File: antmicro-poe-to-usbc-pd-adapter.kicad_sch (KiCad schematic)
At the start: 24 parts, among them J1 Bus_RJ45_5-2337992-8, J2 Bus_RJ45_5-2337992-8, J3 USB-C_WE_632723300011, Q1 PJE138K, U1 TPS2372-3RGWR, U2 LV14540DDAR, U3 STUSB4710AQ1TR, U4 IEA48003A280V-001-R

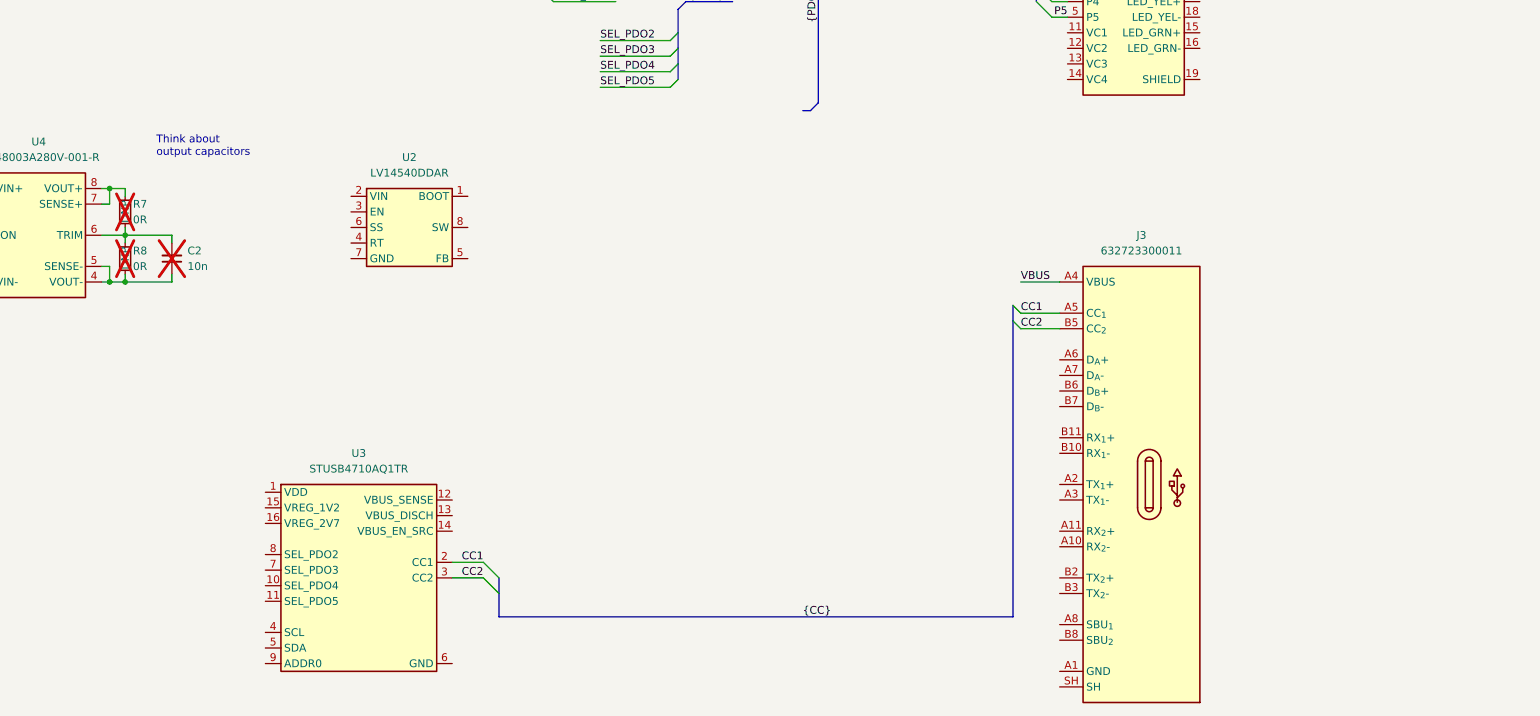
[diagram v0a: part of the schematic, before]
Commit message: [#62182] Connect LV14540
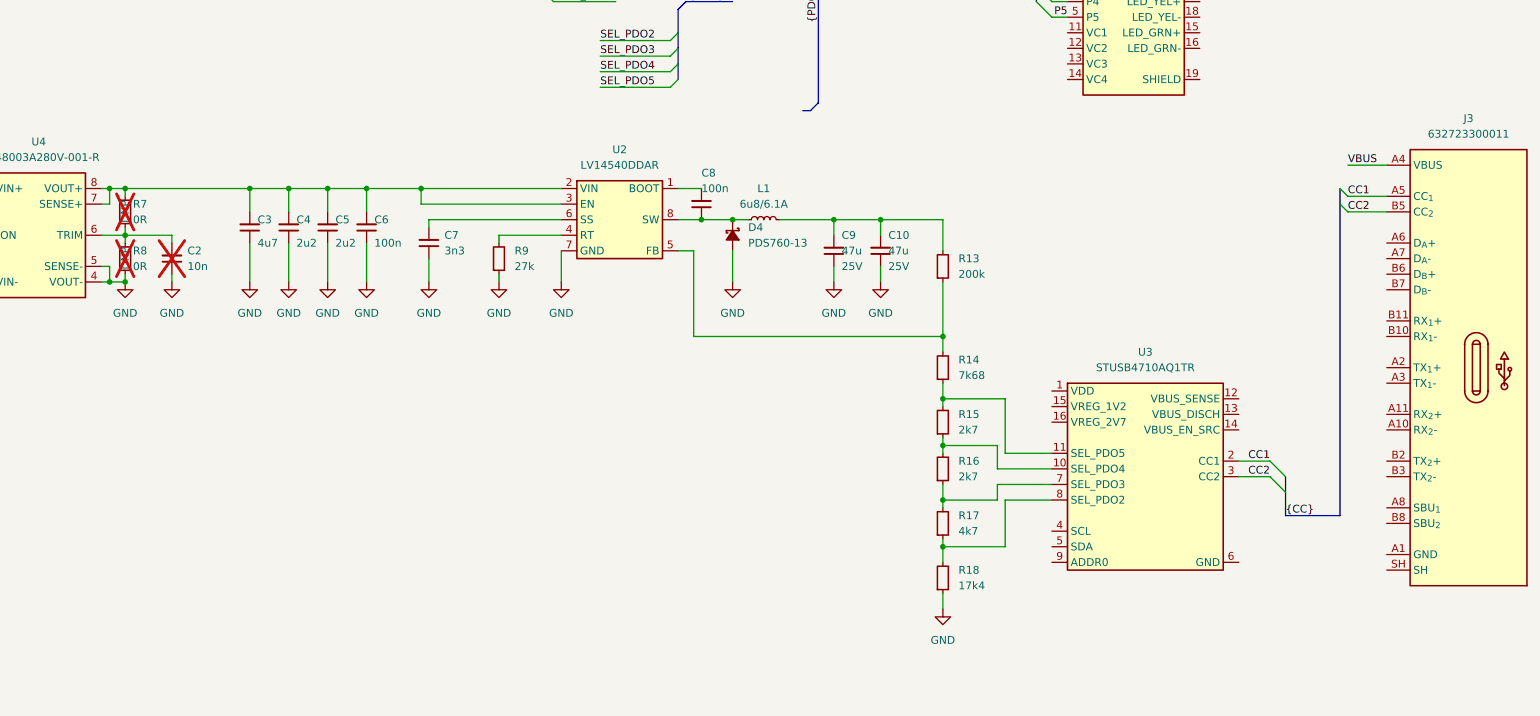
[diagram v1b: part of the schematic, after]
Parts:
- added C10, C9: C_47u_25V_1206, antmicro-footprints:C_1206_3216Metric, symbol antmicroCapacitorsmisc:C_47u_25V_1206
- added C3: C_4u7_1210_100V, antmicro-footprints:C_1210_3225Metric, symbol antmicroCapacitorsmisc:C_4u7_1210_100V
- added C4, C5: C_2u2_1210, antmicro-footprints:C_1210_3225Metric, symbol antmicroCapacitorsmisc:C_2u2_1210
- added C6, C8: C_100n_100V_X7R_0603, antmicro-footprints:C_0603_1608Metric, symbol antmicroCapacitors0603:C_100n_100V_X7R_0603
- added C7: C_3n3_0402, antmicro-footprints:C_0402_1005Metric, symbol antmicroCapacitors0402:C_3n3_0402
- added D4: PDS760, antmicro-footprints:PowerDI5, symbol antmicroDiodesRectifiersSingle:PDS760
- added L1: L_6u8_6.1A_MPS-MPL-AL5050, antmicro-footprints:L_MPS-MPL-AL5050, symbol antmicroFixedInductors:L_6u8_6.1A_MPS-MPL-AL5050
- added R13: R_200k_0402, antmicro-footprints:R_0402_1005Metric, symbol antmicroResistors0402:R_200k_0402
- added R14: R_7k68_0402, antmicro-footprints:R_0402_1005Metric, symbol antmicroResistors0402:R_7k68_0402
- added R15, R16: R_2k7_0402, antmicro-footprints:R_0402_1005Metric, symbol antmicroResistors0402:R_2k7_0402
- added R17: R_4k7_0402, antmicro-footprints:R_0402_1005Metric, symbol antmicroResistors0402:R_4k7_0402
- added R18: R_17k4_0402, antmicro-footprints:R_0402_1005Metric, symbol antmicroResistors0402:R_17k4_0402
- added R9: R_27k_0402, antmicro-footprints:R_0402_1005Metric, symbol antmicroResistors0402:R_27k_0402
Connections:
- net GND: now reaches C2.1, R8.1, U4.4 (VOUT-), U4.5 (SENSE-)
- net GND: now also U2.7 (GND), U2.9 (GND), C10.1, C3.1, C4.1, C5.1, C6.1, C7.1, C9.1, D4.2 (A), R18.1, R9.1
- net at R7.1, U4.7 (SENSE+), U4.8 (VOUT+): now also U2.2 (VIN), U2.3 (EN), C3.2, C4.2, C5.2, C6.2
- net at U3.10 (SEL_PDO4): now also R15.1, R16.2
- net at U3.11 (SEL_PDO5): now also R14.1, R15.2
- net at U3.7 (SEL_PDO3): now also R16.1, R17.2
- net at U3.8 (SEL_PDO2): now also R17.1, R18.2
- net at U2.1 (BOOT): now also C8.2
- net at U2.4 (RT): now also R9.2
- net at U2.5 (FB): now also R13.1, R14.2
- net at U2.6 (SS): now also C7.2
- net at U2.8 (SW): now also C8.1, D4.1 (C), L1.1
- new net: C10.2, C9.2, L1.2, R13.2
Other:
- note removed: "Think about output capacitors"
- moved on the sheet: J3, U2, U3

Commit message: [#62182] Add INA230, remove STUSB4710
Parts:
- removed U3: STUSB4710AQ1TR, antmicro-footprints:QFN-16_3x3mm_P0.5mm, symbol antmicroPMICPowerDistributionSwitchesLoadDrivers:STUSB4710AQ1TR
- added U3: INA230AIRGTR, antmicro-footprints:VQFN-16-1EP_3x3mm_P0.5mm_EP1.68x1.68mm, symbol antmicroPowerMeasurement:INA230AIRGTR
- added U5: FT4232H_VQFN, antmicro-footprints:QFN-56-1EP_8x8mm_P0.5mm, symbol antmicroInterfaceControllers:FT4232H_VQFN
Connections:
- new net: U3.14 (NC), U3.15 (NC), U3.16 (NC), U3.6 (NC), U3.7 (NC), U3.8 (NC)
- new net: U5.16 (V_{CCIO}), U5.36 (V_{CCIO}), U5.50 (V_{CCIO})
- new net: U5.2 (V_{CORE}), U5.31 (V_{CORE})
- new net: U5.21 (GND), U5.41 (GND), U5.45 (GND), U5.57 (GND)
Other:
- note added: "Change for tps25751"
- note added: "Figure 9 example of configuring feedback for buck converter https://www.ti.com/lit/ug/slvubj5/slvubj5.pdf?ts=1720707392282&ref_url=https%253A%252F%252Fwww.ti.com%252Ftool%252FUSB-C-PD-DUO-EVM"
- moved on the sheet: C1, C10, C2, C3, C4, C5, C6, C7, C8, C9, D1, D2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

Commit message: [#62182] Major changes in schematic
Add TPS65987D
Add FT4232H
Add 3v3 buck
Connect components
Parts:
- removed J3: USB-C_WE_632723300011, antmicro-footprints:USB-C_Receptacle_WE_632723300011, symbol antmicroUSBConnectors:USB-C_WE_632723300011
- added C11, C12: C_4u7_0402, d1600e-psu-breakout-board-footprints:0402-cap, symbol d1600e-psu-breakout-board:C_4u7_0402
- added C13, C14: C_100n_0402, d1600e-psu-breakout-board-footprints:0402-cap, symbol d1600e-psu-breakout-board:C_100n_0402
- added C15, C16: C_18p_0402, antmicro-footprints:0402-cap, symbol antmicroCapacitors0402:C_18p_0402
- added C17: C_4u7_1210_100V, antmicro-footprints:C_1210_3225Metric, symbol antmicroCapacitorsmisc:C_4u7_1210_100V
- added C18, C19: C_2u2_1210, antmicro-footprints:C_1210_3225Metric, symbol antmicroCapacitorsmisc:C_2u2_1210
- added C20, C22: C_100n_100V_X7R_0603, antmicro-footprints:C_0603_1608Metric, symbol antmicroCapacitors0603:C_100n_100V_X7R_0603
- added C21: C_3n3_0402, antmicro-footprints:C_0402_1005Metric, symbol antmicroCapacitors0402:C_3n3_0402
- added C23, C24: C_47u_25V_1206, antmicro-footprints:C_1206_3216Metric, symbol antmicroCapacitorsmisc:C_47u_25V_1206
- added C25, C27, C28: C_10u_0402, antmicro-footprints:C_0402_1005Metric, symbol antmicroCapacitors0402:C_10u_0402
- added C26: C_100n_0402, antmicro-footprints:C_0402_1005Metric, symbol antmicroCapacitors0402:C_100n_0402
- added D5: PDS760, antmicro-footprints:PowerDI5, symbol antmicroDiodesRectifiersSingle:PDS760
- added FB1, FB2, FB3: BLM18AG601SN1D, d1600e-psu-breakout-board-footprints:0603, symbol d1600e-psu-breakout-board:BLM18AG601SN1D
- added J3: USB-C_GCT_USB4105-GF-A, antmicro-footprints:USB-C_Receptacle_GCT_USB4105-GF-A, symbol antmicroUSBConnectors:USB-C_GCT_USB4105-GF-A
- added L2: L_6u8_6.1A_MPS-MPL-AL5050, antmicro-footprints:L_MPS-MPL-AL5050, symbol antmicroFixedInductors:L_6u8_6.1A_MPS-MPL-AL5050
- added R19, R20: R_4k7_0402, antmicro-footprints:R_0402_1005Metric, symbol antmicroResistors0402:R_4k7_0402
- added R21: R_12k_0402, antmicro-footprints:R_0402_1005Metric, symbol antmicroResistors0402:R_12k_0402
- added R22, R28: R_0R_0402, antmicro-footprints:R_0402_1005Metric, symbol antmicroResistors0402:R_0R_0402
- added R23: R_1k_0402, antmicro-footprints:R_0402_1005Metric, symbol antmicroResistors0402:R_1k_0402
- added R24: R_27k_0402, antmicro-footprints:R_0402_1005Metric, symbol antmicroResistors0402:R_27k_0402
- added R25: R_200k_0402, antmicro-footprints:R_0402_1005Metric, symbol antmicroResistors0402:R_200k_0402
- added R26: R_59k_0402, antmicro-footprints:R_0402_1005Metric, symbol antmicroResistors0402:R_59k_0402
- added R27: R_0R_2010, antmicro-footprints:R_2010_5025Metric, symbol antmicroResistorsmisc:R_0R_2010
- added R29, R31: R_10k_0402, antmicro-footprints:R_0402_1005Metric, symbol antmicroResistors0402:R_10k_0402
- added R30, R32: R_100k_0402, antmicro-footprints:R_0402_1005Metric, symbol antmicroResistors0402:R_100k_0402
- added U6: TPS65987DDHRSHR, antmicro-footprints:IC_TPS65987DDHRSHR, symbol antmicroInterfaceControllers:TPS65987DDHRSHR
- added U7: LV14540DDAR, antmicro-footprints:SOIC-8-1EP_3.9x4.9x1.75mm_P1.27mm_EP_vias, symbol antmicroDCDCConverters:LV14540DDAR
- added WP1: TP_SMD1MM, d1600e-psu-breakout-board-footprints:Testpoint_smd_1mm, symbol d1600e-psu-breakout-board:TP_SMD1MM
- added Y1: KX-7_12,MHz, d1600e-psu-breakout-board-footprints:KX-7, symbol d1600e-psu-breakout-board:KX-7_12,MHz
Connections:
- net GND: now also U5.10 (TEST), U5.21 (GND), U5.41 (GND), U5.45 (GND), U5.57 (GND), C15.2, C16.2, C17.1, C18.1, C19.1, C20.1, C21.1, C23.1, C24.1, C25.1, C26.2, C27.1, C28.1, D5.2 (A), FB3.2, J3.A1 (GND), J3.A12 (GND), J3.B1 (GND), J3.B12 (GND), R21.1, R24.1, R26.1, R28.1, R30.1, R32.1, U6.20 (GND), U6.45 (GND), U6.46 (GND), U6.47 (GND), U6.51 (GND), U6.59 (GND_EP), U7.7 (GND), U7.9 (GND), Y1.4
- net GNDD: now also C11.2, C12.2, C13.2, C14.2, Y1.2
- net VBUS: now also C10.2, C9.2, L1.2, R13.2
- net +28V: now reaches C3.2, C4.2, C5.2, C6.2, R7.1, U2.2 (VIN), U2.3 (EN), U4.7 (SENSE+), U4.8 (VOUT+)
- net +28V: now also C17.2, C18.2, C19.2, C20.2, U7.2 (VIN), U7.3 (EN)
- net SDA_FTDI: now reaches U3.4 (SDA)
- net SDA_FTDI: now also U5.14 (ADBUS2), R22.2
- net SCL_FTDI: now reaches U3.5 (SCL)
- net SCL_FTDI: now also U5.12 (ADBUS0), R19.1, R20.1
- net FB3: now reaches R16.1, R17.2
- net FB3: now also U6.18 (GPIO2)
- net FB2: now reaches R15.1, R16.2
- net FB2: now also U6.17 (GPIO1)
- net FB1: now reaches R14.1, R15.2
- net FB1: now also U6.16 (GPIO0)
- net FB4: now reaches R17.1, R18.2
- net FB4: now also U6.30 (GPIO3)
- net at U5.11 (~{RESET}): now also R23.2
- net at U5.13 (ADBUS1): now also R22.1
- net WP: now reaches U5.15 (ADBUS3)
- net WP: now also WP1.1
- net +3V3: now reaches U5.16 (V_{CCIO}), U5.36 (V_{CCIO}), U5.50 (V_{CCIO})
- net +3V3: now also U5.44 (V_{REGIN}), C23.2, C24.2, C25.2, C26.1, FB1.2, FB2.2, L2.2, R19.2, R20.2, R23.1, R25.2, U6.5 (VIN_3V3)
- net Vcore: now reaches U5.2 (V_{CORE}), U5.31 (V_{CORE})
- net Vcore: now also U5.43 (V_{REGOUT})
- net OSCI: now reaches U5.3 (OSCI)
- net OSCI: now also C16.1, Y1.3
- net OSCO: now reaches U5.4 (OSCO)
- net OSCO: now also C15.1, Y1.1
- net at U5.5 (V_{PHY}): now also C12.1, C14.1, FB2.1
- net at U5.6 (REF): now also R21.2
- net USB_D+: now reaches U5.7 (D-)
- net USB_D+: now also J3.A6 (D_{A}+)
- net USB_D-: now reaches U5.8 (D+)
- net USB_D-: now also J3.A7 (D_{A}-), J3.B6 (D_{B}+), J3.B7 (D_{B}-)
- net at U5.9 (V_{PLL}): now also C11.1, C13.1, FB1.1
- new net: FB3.1, J3.SH
- new net: C22.1, D5.1 (C), L2.1, U7.8 (SW)
- new net: C22.2, U7.1 (BOOT)
- new net: R25.1, R26.2, U7.5 (FB)
- new net: J3.A4 (VBUS), J3.A9 (VBUS), J3.B4 (VBUS), J3.B9 (VBUS), R27.2, U6.13 (VBUS1)
- new net: J3.A5 (CC_{1}), U6.24 (C1_CC1)
- new net: J3.B5 (CC_{2}), U6.26 (C1_CC2)
- new net: C21.2, U7.6 (SS)
- new net: R24.2, U7.4 (RT)
- new net: R27.1, U6.3 (VBUS2)
- new net DRAIN1: U6.15 (DRAIN1), U6.19 (DRAIN1), U6.58 (DRAIN1), U6.8 (DRAIN1)
- new net DRAIN2: U6.52 (DRAIN2), U6.56 (DRAIN2), U6.57 (DRAIN2), U6.7 (DRAIN2)
- new net PDC_ADCIN1: R29.2, R30.2, U6.6 (ADCIN1)
- new net PDC_ADCIN2: R31.2, R32.2, U6.10 (ADCIN2)
- new net PDC_LDO_1V8: C27.2, U6.35 (LDO_1V8)
- new net PDC_LDO_3V3: C28.2, R29.1, R31.1, U6.9 (LDO_3V3)
- new net PDC_RESET: R28.2, U6.44 (HRESET)
- no-connect marks 5 -> 40
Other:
- note added: "just connect with other pins and make pad as big as possible"
- note removed: "Change for tps25751"
- note removed: "Figure 9 example of configuring feedback for buck converter https://www.ti.com/lit/ug/slvubj5/slvubj5.pdf?ts=1720707392282&ref_url=https%253A%252F%252Fwww.ti.com%252Ftool%252FUSB-C-PD-DUO-EVM"
- moved on the sheet: C1, C10, C2, C3, C4, C5, C6, C7, C8, C9, D1, D2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

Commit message: [#62182] Connect INA230
This is first commit after Meeting #62027
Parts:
- added R33, R34, R35, R36, R37, R38, R39, R40: R_0R_0402, antmicro-footprints:R_0402_1005Metric, symbol antmicroResistors0402:R_0R_0402
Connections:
- net +3V3: now also U3.9 (Vs), R33.2, R37.2
- net GND: now also U3.10 (GND), U3.17 (EP), R36.1, R39.1
- net SCL_FTDI: now also R35.2, R40.2
- net SDA_FTDI: now also R34.2, R38.2
- net VBUS: now also U3.11 (VBUS), U3.13 (IN+)
- net A1: now reaches U3.1 (A1)
- net A1: now also R33.1, R34.1, R35.1, R36.2
- net A0: now reaches U3.2 (A0)
- net A0: now also R37.1, R38.1, R39.2, R40.1
- no-connect marks 40 -> 41
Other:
- note removed: "Read more about Ferrite Beads"
- moved on the sheet: FB3, J3, R27, U3, U6B

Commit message: [#62182] Change passives, correct gnd
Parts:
- removed C11, C12: C_4u7_0402, d1600e-psu-breakout-board-footprints:0402-cap, symbol d1600e-psu-breakout-board:C_4u7_0402
- removed C13, C14: C_100n_0402, d1600e-psu-breakout-board-footprints:0402-cap, symbol d1600e-psu-breakout-board:C_100n_0402
- removed C15, C16: C_18p_0402, antmicro-footprints:0402-cap, symbol antmicroCapacitors0402:C_18p_0402
- removed FB1, FB2, FB3: BLM18AG601SN1D, d1600e-psu-breakout-board-footprints:0603, symbol d1600e-psu-breakout-board:BLM18AG601SN1D
- removed WP1: TP_SMD1MM, d1600e-psu-breakout-board-footprints:Testpoint_smd_1mm, symbol d1600e-psu-breakout-board:TP_SMD1MM
- removed Y1: KX-7_12,MHz, d1600e-psu-breakout-board-footprints:KX-7, symbol d1600e-psu-breakout-board:KX-7_12,MHz
- added C11, C29: C_4u7_25V_0402, antmicro-footprints:C_0402_1005Metric, symbol antmicroCapacitors0402:C_4u7_25V_0402
- added C12, C30: C_100n_16V_X7R_0402, antmicro-footprints:C_0402_1005Metric, symbol antmicroCapacitors0402:C_100n_16V_X7R_0402
- added C13, C14: C_18p_0402, antmicro-footprints:C_0402_1005Metric, symbol antmicroCapacitors0402:C_18p_0402
- added FB1, FB4, FB5: FB_600Z_0.5A_Murata-BLM18AG_0603, antmicro-footprints:FB_0603_1608Metric, symbol antmicroFerriteBeadsandChips:FB_600Z_0.5A_Murata-BLM18AG_0603
- added TP1: TP_1.5mm_SMD, antmicro-footprints:TP_SMD_1.5mm, symbol antmicroTestPoints:TP_1.5mm_SMD
- added Y1: Resonator_12MHz_ABM8G, antmicro-footprints:Resonator_SMD_Abracon_ABM8G_3.2x2.5mm, symbol antmicroResonators:Resonator_12MHz_ABM8G
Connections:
- net +3V3: now also FB4.1, FB5.1
- net GND: now also C11.1, C12.1, C13.1, C14.1, C29.1, C30.1, FB1.2, Y1.2 (SH), Y1.4 (SH)
- net OSCI: now also C14.2, Y1.3
- net OSCO: now also C13.2, Y1.1
- net WP: now also TP1.1
- net at U5.9 (V_{PLL}): now also C29.2, C30.2, FB4.2
- net at J3.SH: now also FB1.1
- net at U5.5 (V_{PHY}): now also C11.2, C12.2, FB5.2
